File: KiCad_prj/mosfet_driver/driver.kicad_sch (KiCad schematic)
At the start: 26 parts, among them U3 UCC21520ADW

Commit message: Mosfet driver v rev. 1.0 odeslan do vyroby
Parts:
- C10, C11, C12, C7, C8, C9: JLCPCB Part # (none) -> C28323
- C3: JLCPCB Part # (none) -> C1743
- C4, C5, C6: JLCPCB Part # (none) -> C1804
- D1, D2: JLCPCB Part # (none) -> C2480
- R10, R12: JLCPCB Part # (none) -> C16257
- R11, R13: JLCPCB Part # (none) -> C17415
- R14, R15, R6, R7, R8: JLCPCB Part # (none) -> C17414
- R3, R4, R5: JLCPCB Part # (none) -> C17408
- R9: JLCPCB Part # (none) -> C17713
- U3: JLCPCB Part # (none) -> C2863027
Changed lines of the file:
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@@
+			)
+		)
+		(property "JLCPCB Part #" "C17415"
+			(at 203.2 104.14 90)
+			(effects
+				(font
+					(size 1.27 1.27)
+				)
+				(hide yes)
 			)
 		)
@@
 			)
 		)
+		(property "JLCPCB Part #" "C17414"
+			(at 58.42 104.14 0)
+			(effects
+				(font
+					(size 1.27 1.27)
+				)
+				(hide yes)
+			)
+		)
 		(pin "1"
 		)
@@
 		(exclude_from_sim no)
 		(in_bom yes)
-		(on_board no)
+		(on_board yes)
 		(dnp no)
 		(fields_autoplaced yes)
@@
 			)
 		)
+		(property "JLCPCB Part #" "C17414"
+			(at 234.95 93.98 90)
+			(effects
+				(font
+					(size 1.27 1.27)
+				)
+				(hide yes)
+			)
+		)
 		(pin "1"
 		)
@@
 			)
 		)
+		(property "JLCPCB Part #" "C1804"
+			(at 68.58 104.14 0)
+			(effects
+				(font
+					(size 1.27 1.27)
+				)
+				(hide yes)
+			)
+		)
 		(pin "2"
 		)
@@
 			)
 		)
+		(property "JLCPCB Part #" "C28323"
+			(at 149.86 128.27 0)
+			(effects
+				(font
+					(size 1.27 1.27)
+				)
+				(hide yes)
+			)
+		)
 		(pin "1"
 		)
@@
 			)
 		)
+		(property "JLCPCB Part #" "C17415"
+			(at 203.2 129.54 90)
+			(effects
+				(font
+					(size 1.27 1.27)
+				)
+				(hide yes)
+			)
+		)
 		(pin "1"
 		)
@@
 			)
 		)
+		(property "JLCPCB Part #" "C17713"
+			(at 68.58 123.19 0)
+			(effects
+				(font
+					(size 1.27 1.27)
+				)
+				(hide yes)
+			)
+		)
 		(pin "1"
 		)
@@
 			)
 		)
+		(property "JLCPCB Part #" "C17408"
+			(at 50.8 100.33 90)
+			(effects
+				(font
+					(size 1.27 1.27)
+				)
+				(hide yes)
+			)
+		)
 		(pin "1"
 		)
@@
 			)
 		)
+		(property "JLCPCB Part #" "C1804"
+			(at 68.58 60.96 0)
+			(effects
+				(font
+					(size 1.27 1.27)
+				)
+				(hide yes)
+			)
+		)
 		(pin "2"
 		)
@@
 		(exclude_from_sim no)
 		(in_bom yes)
-		(on_board no)
+		(on_board yes)
 		(dnp no)
 		(fields_autoplaced yes)
@@
 			)
 		)
+		(property "JLCPCB Part #" "C17414"
+			(at 234.95 119.38 90)
+			(effects
+				(font
+					(size 1.27 1.27)
+				)
+				(hide yes)
+			)
+		)
 		(pin "1"
 		)
@@
 			)
 		)
+		(property "JLCPCB Part #" "C28323"
+			(at 114.3 101.6 90)
+			(effects
+				(font
+					(size 1.27 1.27)
+				)
+				(hide yes)
+			)
+		)
 		(pin "1"
 		)
@@
 			)
 		)
+		(property "JLCPCB Part #" "C2480"
+			(at 227.33 93.98 0)
+			(effects
+				(font
+					(size 1.27 1.27)
+				)
+				(hide yes)
+			)
+		)
 		(pin "1"
 		)
@@
 			)
 		)
+		(property "JLCPCB Part #" "C1743"
+			(at 58.42 123.19 0)
+			(effects
+				(font
+					(size 1.27 1.27)
+				)
+				(hide yes)
+			)
+		)
 		(pin "1"
 		)
@@
 			)
 		)
+		(property "JLCPCB Part #" "C17408"
+			(at 50.8 57.15 90)
+			(effects
+				(font
+					(size 1.27 1.27)
+				)
+				(hide yes)
+			)
+		)
 		(pin "1"
 		)
@@
 			)
 		)
+		(property "JLCPCB Part #" "C28323"
+			(at 162.56 96.52 0)
+			(effects
+				(font
+					(size 1.27 1.27)
+				)
+				(hide yes)
+			)
+		)
 		(pin "1"
 		)
@@
 			)
 		)
+		(property "JLCPCB Part #" "C28323"
+			(at 114.3 90.17 90)
+			(effects
+				(font
+					(size 1.27 1.27)
+				)
+				(hide yes)
+			)
+		)
 		(pin "1"
 		)
@@
 			)
 		)
+		(property "JLCPCB Part #" "C2480"
+			(at 227.33 119.38 0)
+			(effects
+				(font
+					(size 1.27 1.27)
+				)
+				(hide yes)
+			)
+		)
 		(pin "1"
 		)
@@
 			)
 		)
+		(property "JLCPCB Part #" "C16257"
+			(at 203.2 93.98 90)
+			(effects
+				(font
+					(size 1.27 1.27)
+				)
+				(hide yes)
+			)
+		)
 		(pin "1"
 		)
@@
 			)
 		)
+		(property "JLCPCB Part #" "C28323"
+			(at 162.56 128.27 0)
+			(effects
+				(font
+					(size 1.27 1.27)
+				)
+				(hide yes)
+			)
+		)
 		(pin "1"
 		)
@@
 			)
 		)
+		(property "JLCPCB Part #" "C17408"
+			(at 50.8 78.74 90)
+			(effects
+				(font
+					(size 1.27 1.27)
+				)
+				(hide yes)
+			)
+		)
 		(pin "1"
 		)
@@
 			)
 		)
+		(property "JLCPCB Part #" "C1804"
+			(at 68.58 82.55 0)
+			(effects
+				(font
+					(size 1.27 1.27)
+				)
+				(hide yes)
+			)
+		)
 		(pin "2"
 		)
@@
 			)
 		)
+		(property "JLCPCB Part #" "C2863027"
+			(at 132.08 111.76 0)
+			(effects
+				(font
+					(size 1.27 1.27)
+				)
+				(hide yes)
+			)
+		)
 		(pin "1"
 		)
@@
 			)
 		)
+		(property "JLCPCB Part #" "C17414"
+			(at 58.42 60.96 0)
+			(effects
+				(font
+					(size 1.27 1.27)
+				)
+				(hide yes)
+			)
+		)
 		(pin "1"
 		)
@@
 			)
 		)
+		(property "JLCPCB Part #" "C28323"
+			(at 149.86 96.52 0)
+			(effects
+				(font
+					(size 1.27 1.27)
+				)
+				(hide yes)
+			)
+		)
 		(pin "1"
 		)
@@
 			)
 		)
+		(property "JLCPCB Part #" "C17414"
+			(at 58.42 82.55 0)
+			(effects
+				(font
+					(size 1.27 1.27)
+				)
+				(hide yes)
+			)
+		)
 		(pin "1"
 		)
@@
 			(effects
 				(font
+					(size 1.27 1.27)
+				)
+				(hide yes)
+			)
+		)
+		(property "JLCPCB Part #" "C16257"
+			(at 203.2 119.38 90)
+			(effects
+				(font

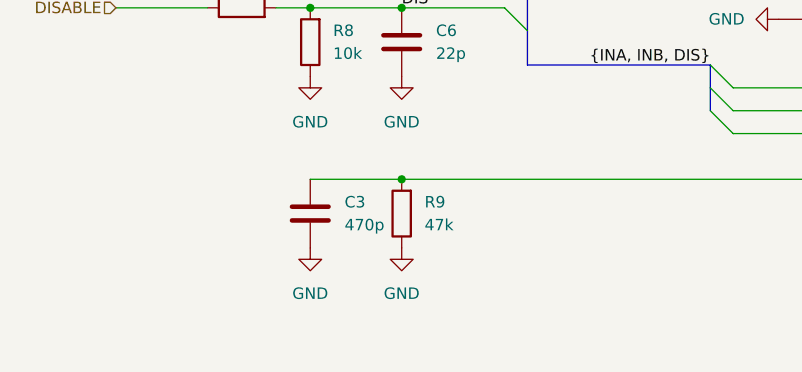
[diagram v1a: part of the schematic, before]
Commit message: Oprava budice na zaklade vysledku zkousek, pridano drazkovani
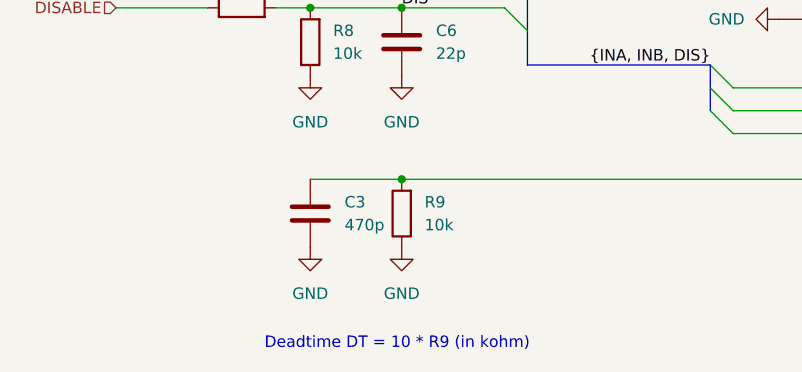
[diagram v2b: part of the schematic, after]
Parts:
- R9: value 47k -> 10k; JLCPCB Part # C17713 -> C17414
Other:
- note added: "Deadtime DT = 10 * R9 (in kohm)"
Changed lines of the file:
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@@
 		(rev "${REVISION}")
+	)
+	(text "Deadtime DT = 10 * R9 (in kohm)"
+		(exclude_from_sim no)
+		(at 68.072 137.668 0)
+		(effects
+			(font
+				(size 1.27 1.27)
+			)
+		)
 	)
 	(junction
@@
 	(wire
 		(pts
+			(xy 68.58 119.38) (xy 119.38 119.38)
+		)
+		(stroke
+			(width 0)
+			(type default)
+		)
+	)
+	(wire
+		(pts
 			(xy 58.42 78.74) (xy 68.58 78.74)
 		)
@@
 	(wire
 		(pts
+			(xy 162.56 132.08) (xy 162.56 133.35)
+		)
+		(stroke
+			(width 0)
+			(type default)
+		)
+	)
+	(wire
+		(pts
+			(xy 149.86 123.19) (xy 172.72 123.19)
+		)
+		(stroke
+			(width 0)
+			(type default)
+		)
+	)
+	(wire
+		(pts
+			(xy 149.86 123.19) (xy 149.86 121.92)
+		)
+		(stroke
+			(width 0)
+			(type default)
+		)
+	)
+	(wire
+		(pts
+			(xy 231.14 93.98) (xy 231.14 104.14)
+		)
+		(stroke
+			(width 0)
+			(type default)
+		)
+	)
+	(wire
+		(pts
+			(xy 118.11 101.6) (xy 119.38 101.6)
+		)
+		(stroke
+			(width 0)
+			(type default)
+		)
+	)
+	(wire
+		(pts
+			(xy 207.01 119.38) (xy 223.52 119.38)
+		)
+		(stroke
+			(width 0)
+			(type default)
+		)
+	)
+	(wire
+		(pts
+			(xy 54.61 100.33) (xy 58.42 100.33)
+		)
+		(stroke
+			(width 0)
+			(type default)
+		)
+	)
+	(wire
+		(pts
+			(xy 207.01 93.98) (xy 223.52 93.98)
+		)
+		(stroke
+			(width 0)
+			(type default)
+		)
+	)
+	(wire
+		(pts
+			(xy 231.14 119.38) (xy 231.14 129.54)
+		)
+		(stroke
+			(width 0)
+			(type default)
+		)
+	)
+	(wire
+		(pts
 			(xy 58.42 119.38) (xy 68.58 119.38)
-		)
-		(stroke
-			(width 0)
-			(type default)
-		)
-	)
-	(wire
-		(pts
-			(xy 162.56 132.08) (xy 162.56 133.35)
-		)
-		(stroke
-			(width 0)
-			(type default)
-		)
-	)
-	(wire
-		(pts
-			(xy 149.86 123.19) (xy 172.72 123.19)
-		)
-		(stroke
-			(width 0)
-			(type default)
-		)
-	)
-	(wire
-		(pts
-			(xy 149.86 123.19) (xy 149.86 121.92)
-		)
-		(stroke
-			(width 0)
-			(type default)
-		)
-	)
-	(wire
-		(pts
-			(xy 231.14 93.98) (xy 231.14 104.14)
-		)
-		(stroke
-			(width 0)
-			(type default)
-		)
-	)
-	(wire
-		(pts
-			(xy 118.11 101.6) (xy 119.38 101.6)
-		)
-		(stroke
-			(width 0)
-			(type default)
-		)
-	)
-	(wire
-		(pts
-			(xy 207.01 119.38) (xy 223.52 119.38)
-		)
-		(stroke
-			(width 0)
-			(type default)
-		)
-	)
-	(wire
-		(pts
-			(xy 54.61 100.33) (xy 58.42 100.33)
-		)
-		(stroke
-			(width 0)
-			(type default)
-		)
-	)
-	(wire
-		(pts
-			(xy 207.01 93.98) (xy 223.52 93.98)
-		)
-		(stroke
-			(width 0)
-			(type default)
-		)
-	)
-	(wire
-		(pts
-			(xy 231.14 119.38) (xy 231.14 129.54)
-		)
-		(stroke
-			(width 0)
-			(type default)
-		)
-	)
-	(wire
-		(pts
-			(xy 68.58 119.38) (xy 119.38 119.38)
 		)
 		(stroke
@@
 	)
 	(symbol
-		(lib_id "Device:R")
-		(at 68.58 123.19 180)
-		(unit 1)
-		(exclude_from_sim no)
-		(in_bom yes)
-		(on_board yes)
-		(dnp no)
-		(fields_autoplaced yes)
-		(property "Reference" "R9"
-			(at 71.12 121.9199 0)
-			(effects
-				(font
-					(size 1.27 1.27)
-				)
-				(justify right)
-			)
-		)
-		(property "Value" "47k"
-			(at 71.12 124.4599 0)
-			(effects
-				(font
-					(size 1.27 1.27)
-				)
-				(justify right)
-			)
-		)
-		(property "Footprint" "Resistor_SMD:R_0805_2012Metric"
-			(at 70.358 123.19 90)
-			(effects
-				(font
-					(size 1.27 1.27)
-				)
-				(hide yes)
-			)
-		)
-		(property "Datasheet" "~"
-			(at 68.58 123.19 0)
-			(effects
-				(font
-					(size 1.27 1.27)
-				)
-				(hide yes)
-			)
-		)
-		(property "Description" "Resistor"
-			(at 68.58 123.19 0)
-			(effects
-				(font
-					(size 1.27 1.27)
-				)
-				(hide yes)
-			)
-		)
-		(property "JLCPCB Part #" "C17713"
-			(at 68.58 123.19 0)
-			(effects
-				(font
-					(size 1.27 1.27)
-				)
-				(hide yes)
-			)
-		)
-		(pin "1"
-		)
-		(pin "2"
-		)
-		(instances
-			(project "Mosfet_driver"
-				(path "/affe9f01-beaf-4b8a-b5ac-1888fb444f62/3d388a56-2466-4d51-8971-3f7a4f39f3a1"
-					(reference "R9")
-					(unit 1)
-				)
-			)
-		)
-	)
-	(symbol
 		(lib_id "power:GND")
 		(at 68.58 64.77 0)
@@
 					(unit 1)
 				)
+			)
+		)
+	)
+	(symbol
+		(lib_id "Device:R")
+		(at 68.58 123.19 180)
+		(unit 1)
+		(exclude_from_sim no)
+		(in_bom yes)
+		(on_board yes)
+		(dnp no)
+		(fields_autoplaced yes)
+		(property "Reference" "R9"
+			(at 71.12 121.9199 0)
+			(effects
+				(font
+					(size 1.27 1.27)
+				)
+				(justify right)
+			)
+		)
+		(property "Value" "10k"
+			(at 71.12 124.4599 0)
+			(effects
+				(font
+					(size 1.27 1.27)
+				)
+				(justify right)
+			)
+		)
+		(property "Footprint" "Resistor_SMD:R_0805_2012Metric"
+			(at 70.358 123.19 90)
+			(effects
+				(font
+					(size 1.27 1.27)
+				)
+				(hide yes)
+			)
+		)
+		(property "Datasheet" "~"
+			(at 68.58 123.19 0)
+			(effects
+				(font
+					(size 1.27 1.27)
+				)
+				(hide yes)
+			)
+		)
+		(property "Description" "Resistor"
+			(at 68.58 123.19 0)
+			(effects
+				(font
+					(size 1.27 1.27)
+				)
+				(hide yes)
+			)
+		)
+		(property "JLCPCB Part #" "C17414"
+			(at 68.58 123.19 0)
+			(effects
+				(font
+					(size 1.27 1.27)
+				)
+				(hide yes)
+			)
+		)
+		(pin "1"
+		)
+		(pin "2"
+		)
+		(instances
+			(project "mosfet_driver"
+				(path "/affe9f01-beaf-4b8a-b5ac-1888fb444f62/3d388a56-2466-4d51-8971-3f7a4f39f3a1"
+					(reference "R9")
+					(unit 1)
+				)
